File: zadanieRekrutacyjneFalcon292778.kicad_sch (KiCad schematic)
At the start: 65 parts, among them J1 Conn_01x03_Pin, J2 Conn_01x02_Pin, J3 Conn_01x02_Pin, J4 Conn_01x04_Pin, J5 Conn_01x08_Pin, J6 Conn_01x08_Pin, J7 Conn_01x02_Pin, SW1 CK_KMS2xxG, SW2 SW_Nidec_CAS-120A1, SW3 CK_KMS2xxG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

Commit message: placement + testowy tracking v1
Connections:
- net JTAGCLK: now also J4.1 (Pin_1); no longer J4.2 (Pin_2)
- net JTAGI: now also J4.3 (Pin_3); no longer J4.4 (Pin_4)
- net JTAGMS: now also J4.4 (Pin_4); no longer J4.1 (Pin_1)
- net JTAGO: now also J4.2 (Pin_2); no longer J4.3 (Pin_3)
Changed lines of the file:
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@@
-		)
-	)
-	(label "JTAGI"
-		(at 369.57 105.41 0)
-		(effects
-			(font
-				(size 1.27 1.27)
-			)
-			(justify left bottom)
 		)
 	)
@@
 		)
 	)
+	(label "JTAGI"
+		(at 369.57 102.87 0)
+		(effects
+			(font
+				(size 1.27 1.27)
+			)
+			(justify left bottom)
+		)
+	)
 	(label "SPI2"
 		(at 270.51 198.12 180)
@@
 		)
 	)
-	(label "JTAGCLK"
-		(at 369.57 100.33 0)
-		(effects
-			(font
-				(size 1.27 1.27)
-			)
-			(justify left bottom)
-		)
-	)
 	(label "JTAGO"
 		(at 190.5 86.36 0)
@@
 		)
 	)
-	(label "JTAGO"
-		(at 369.57 102.87 0)
-		(effects
-			(font
-				(size 1.27 1.27)
-			)
-			(justify left bottom)
-		)
-	)
 	(label "GPIO1"
 		(at 142.24 68.58 180)
@@
 		)
 	)
+	(label "JTAGCLK"
+		(at 369.57 97.79 0)
+		(effects
+			(font
+				(size 1.27 1.27)
+			)
+			(justify left bottom)
+		)
+	)
 	(label "SPICLK"
 		(at 270.51 190.5 180)
@@
 		)
 	)
-	(label "JTAGMS"
-		(at 369.57 97.79 0)
-		(effects
-			(font
-				(size 1.27 1.27)
-			)
-			(justify left bottom)
-		)
-	)
 	(label "IMUData"
 		(at 312.42 53.34 0)
@@
 		)
 	)
+	(label "JTAGMS"
+		(at 369.57 105.41 0)
+		(effects
+			(font
+				(size 1.27 1.27)
+			)
+			(justify left bottom)
+		)
+	)
 	(label "GPIO2"
 		(at 142.24 71.12 180)
@@
 		(effects
 			(font
+				(size 1.27 1.27)
+			)
+			(justify left bottom)
+		)
+	)
+	(label "JTAGO"
+		(at 369.57 100.33 0)
+		(effects
+			(font

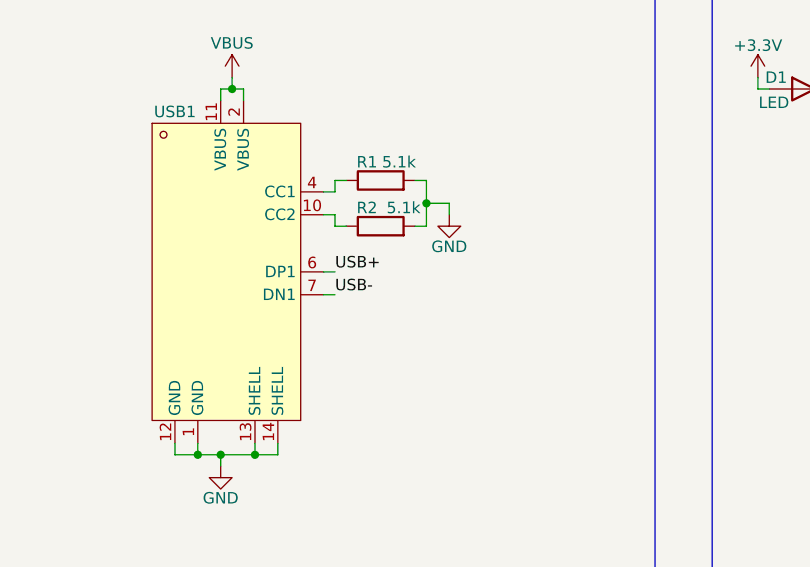
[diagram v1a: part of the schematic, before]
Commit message: zroutowane (do poprawy footprinty, DRC)
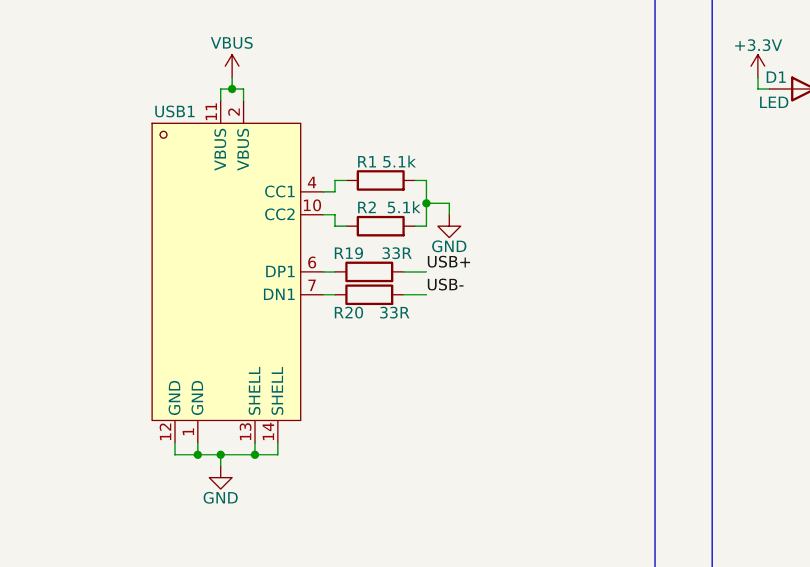
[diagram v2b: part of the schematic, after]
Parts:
- added R19, R20: 33R, Resistor_SMD:R_0603_1608Metric, symbol Device:R
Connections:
- net USB+: now also R19.2; no longer USB1.6 (DP1)
- net USB-: now also R20.2; no longer USB1.7 (DN1)
- new net: R19.1, USB1.6 (DP1)
- new net: R20.1, USB1.7 (DN1)
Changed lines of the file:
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@@
 	(wire
 		(pts
+			(xy 73.66 55.88) (xy 76.2 55.88)
+		)
+		(stroke
+			(width 0)
+			(type default)
+		)
+	)
+	(wire
+		(pts
 			(xy 189.23 86.36) (xy 190.5 86.36)
 		)
@@
 	(wire
 		(pts
+			(xy 73.66 53.34) (xy 76.2 53.34)
+		)
+		(stroke
+			(width 0)
+			(type default)
+		)
+	)
+	(wire
+		(pts
 			(xy 76.2 48.26) (xy 76.2 45.72)
 		)
@@
 	)
 	(label "USB-"
-		(at 66.04 55.88 0)
+		(at 76.2 55.88 0)
 		(effects
 			(font
@@
 	)
 	(label "USB+"
-		(at 66.04 53.34 0)
+		(at 76.2 53.34 0)
 		(effects
 			(font
@@
 	)
 	(symbol
+		(lib_id "Device:R")
+		(at 69.85 53.34 90)
+		(unit 1)
+		(exclude_from_sim no)
+		(in_bom yes)
+		(on_board yes)
+		(dnp no)
+		(property "Reference" "R19"
+			(at 67.564 51.308 90)
+			(effects
+				(font
+					(size 1.27 1.27)
+				)
+			)
+		)
+		(property "Value" "33R"
+			(at 72.898 51.308 90)
+			(effects
+				(font
+					(size 1.27 1.27)
+				)
+			)
+		)
+		(property "Footprint" "Resistor_SMD:R_0603_1608Metric"
+			(at 69.85 55.118 90)
+			(effects
+				(font
+					(size 1.27 1.27)
+				)
+				(hide yes)
+			)
+		)
+		(property "Datasheet" "~"
+			(at 69.85 53.34 0)
+			(effects
+				(font
+					(size 1.27 1.27)
+				)
+				(hide yes)
+			)
+		)
+		(property "Description" "Resistor"
+			(at 69.85 53.34 0)
+			(effects
+				(font
+					(size 1.27 1.27)
+				)
+				(hide yes)
+			)
+		)
+		(pin "1"
+		)
+		(pin "2"
+		)
+		(instances
+			(project "zadanieRekrutacyjneFalcon292778"
+				(path "/b0ec743d-f62d-4025-8f04-7134197de925"
+					(reference "R19")
+					(unit 1)
+				)
+			)
+		)
+	)
+	(symbol
 		(lib_id "Device:C")
 		(at 59.69 198.12 0)
@@
 					(unit 1)
 				)
+			)
+		)
+	)
+	(symbol
+		(lib_id "Device:R")
+		(at 69.85 55.88 90)
+		(unit 1)
+		(exclude_from_sim no)
+		(in_bom yes)
+		(on_board yes)
+		(dnp no)
+		(property "Reference" "R20"
+			(at 67.564 57.912 90)
+			(effects
+				(font
+					(size 1.27 1.27)
+				)
+			)
+		)
+		(property "Value" "33R"
+			(at 72.644 57.912 90)
+			(effects
+				(font
+					(size 1.27 1.27)
+				)
+			)
+		)
+		(property "Footprint" "Resistor_SMD:R_0603_1608Metric"
+			(at 69.85 57.658 90)
+			(effects
+				(font
+					(size 1.27 1.27)
+				)
+				(hide yes)
+			)
+		)
+		(property "Datasheet" "~"
+			(at 69.85 55.88 0)
+			(effects
+				(font
+					(size 1.27 1.27)
+				)
+				(hide yes)
+			)
+		)
+		(property "Description" "Resistor"
+			(at 69.85 55.88 0)
+			(effects
+				(font
+					(size 1.27 1.27)
+				)
+				(hide yes)
+			)
+		)
+		(pin "1"
+		)
+		(pin "2"
+		)
+		(instances
+			(project "zadanieRekrutacyjneFalcon292778"
+				(path "/b0ec743d-f62d-4025-8f04-7134197de925"
+					(reference "R20")
+					(unit 1)
+				)

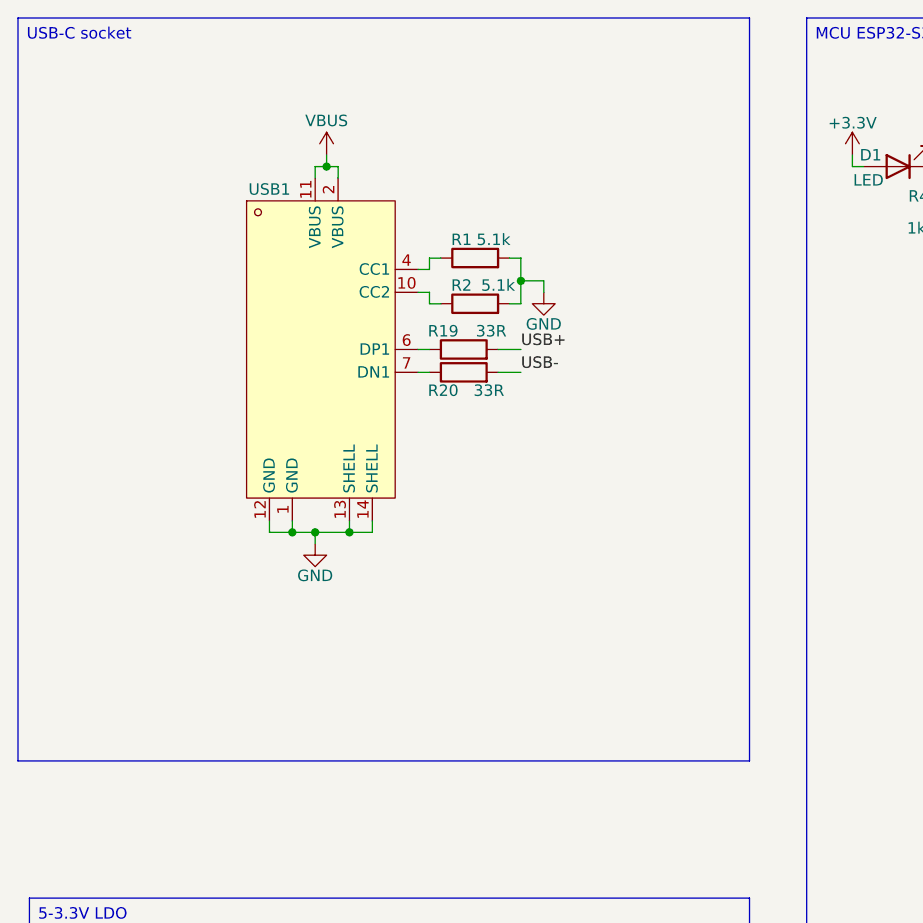
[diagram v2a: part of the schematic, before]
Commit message: DRC naprawione 3d modele dodane, transile dodane
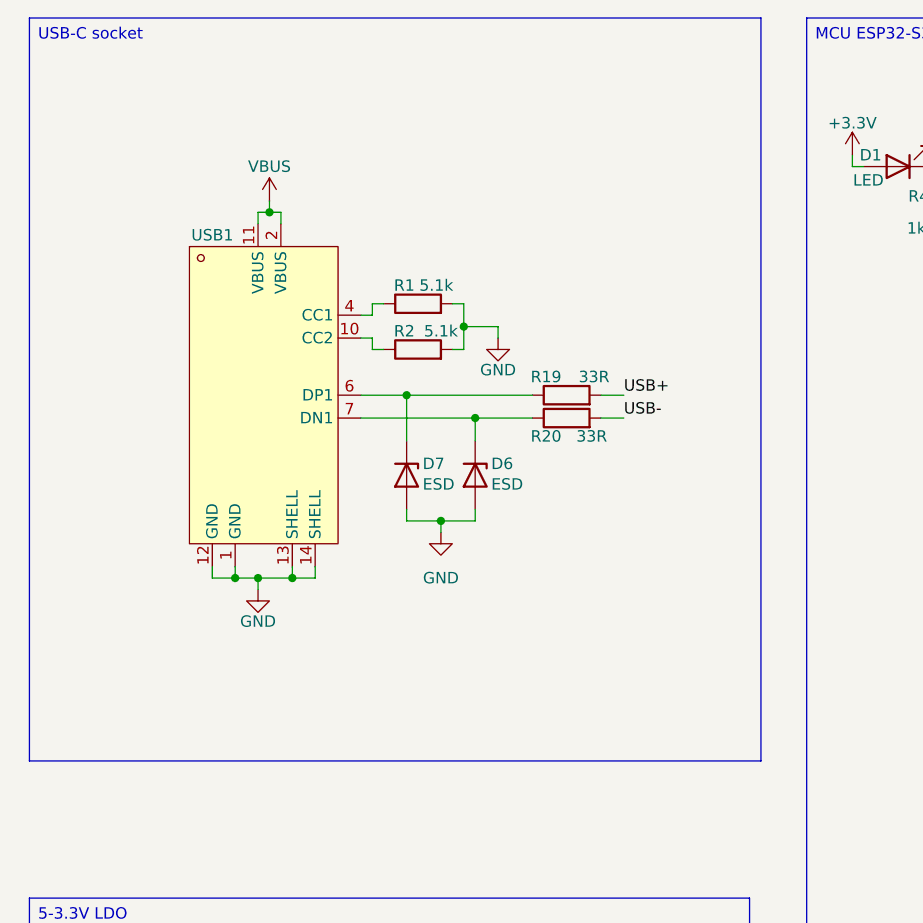
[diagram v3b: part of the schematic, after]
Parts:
- added D6, D7: ESD, Diode_SMD:D_SOD-523, symbol Diode:ESD5Zxx
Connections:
- net GND: now also D6.2 (A), D7.2 (A)
- net at R19.1, USB1.6 (DP1): now also D7.1 (K)
- net at R20.1, USB1.7 (DN1): now also D6.1 (K)
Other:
- moved on the sheet: R1, R19, R2, R20, USB1

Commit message: Finalna wersja v1
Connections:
- net GND: now also AE1.2 (GND)
- net Wi-Fi: no longer D2.2 (A2)
- net at AE1.1 (A), C14.1, L2.1: now also D2.2 (A2)
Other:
- moved on the sheet: C14, C15, D2, L2
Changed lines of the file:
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@@
 	)
 	(junction
+		(at 154.94 203.2)
+		(diameter 0)
+		(color 0 0 0 0)
+	)
+	(junction
 		(at 48.26 38.1)
 		(diameter 0)
@@
 	)
 	(junction
-		(at 165.1 193.04)
-		(diameter 0)
-		(color 0 0 0 0)
-	)
-	(junction
 		(at 69.85 132.08)
 		(diameter 0)
@@
 	)
 	(junction
-		(at 165.1 203.2)
+		(at 163.83 203.2)
 		(diameter 0)
 		(color 0 0 0 0)
@@
 	)
 	(junction
+		(at 163.83 193.04)
+		(diameter 0)
+		(color 0 0 0 0)
+	)
+	(junction
 		(at 39.37 193.04)
 		(diameter 0)
@@
 	)
 	(junction
+		(at 154.94 193.04)
+		(diameter 0)
+		(color 0 0 0 0)
+	)
+	(junction
 		(at 46.99 78.74)
 		(diameter 0)
@@
 	)
 	(junction
-		(at 154.94 193.04)
-		(diameter 0)
-		(color 0 0 0 0)
-	)
-	(junction
 		(at 67.31 72.39)
 		(diameter 0)
@@
 	(wire
 		(pts
-			(xy 173.99 194.31) (xy 173.99 193.04)
-		)
-		(stroke
-			(width 0)
-			(type default)
-		)
-	)
-	(wire
-		(pts
 			(xy 300.99 52.07) (xy 300.99 53.34)
 		)
@@
 	(wire
 		(pts
-			(xy 154.94 193.04) (xy 154.94 194.31)
+			(xy 163.83 193.04) (xy 163.83 194.31)
 		)
 		(stroke
@@
 	(wire
 		(pts
-			(xy 154.94 201.93) (xy 154.94 203.2)
+			(xy 163.83 201.93) (xy 163.83 203.2)
 		)
 		(stroke
@@
 	(wire
 		(pts
-			(xy 154.94 193.04) (xy 156.21 193.04)
+			(xy 123.19 48.26) (xy 123.19 49.53)
 		)
 		(stroke
@@
 	(wire
 		(pts
-			(xy 123.19 48.26) (xy 123.19 49.53)
+			(xy 281.94 175.26) (xy 281.94 177.8)
 		)
 		(stroke
@@
 	(wire
 		(pts
-			(xy 281.94 175.26) (xy 281.94 177.8)
+			(xy 189.23 83.82) (xy 190.5 83.82)
 		)
 		(stroke
@@
 	(wire
 		(pts
-			(xy 189.23 83.82) (xy 190.5 83.82)
+			(xy 68.58 193.04) (xy 68.58 194.31)
 		)
 		(stroke
@@
 	(wire
 		(pts
-			(xy 68.58 193.04) (xy 68.58 194.31)
+			(xy 44.45 78.74) (xy 46.99 78.74)
 		)
 		(stroke
@@
 	(wire
 		(pts
-			(xy 44.45 78.74) (xy 46.99 78.74)
+			(xy 189.23 88.9) (xy 190.5 88.9)
 		)
 		(stroke
@@
 	(wire
 		(pts
-			(xy 189.23 88.9) (xy 190.5 88.9)
+			(xy 173.99 203.2) (xy 170.18 203.2)
 		)
 		(stroke
@@
 	(wire
 		(pts
-			(xy 154.94 203.2) (xy 165.1 203.2)
+			(xy 163.83 203.2) (xy 170.18 203.2)
 		)
 		(stroke
@@
 	(wire
 		(pts
-			(xy 163.83 193.04) (xy 165.1 193.04)
+			(xy 172.72 193.04) (xy 173.99 193.04)
 		)
 		(stroke
@@
 	(wire
 		(pts
-			(xy 173.99 193.04) (xy 165.1 193.04)
+			(xy 142.24 66.04) (xy 143.51 66.04)
 		)
 		(stroke
@@
 	(wire
 		(pts
-			(xy 142.24 66.04) (xy 143.51 66.04)
+			(xy 142.24 68.58) (xy 143.51 68.58)
 		)
 		(stroke
@@
 	(wire
 		(pts
-			(xy 142.24 68.58) (xy 143.51 68.58)
+			(xy 152.4 203.2) (xy 154.94 203.2)
 		)
 		(stroke
@@
 	(wire
 		(pts
-			(xy 165.1 193.04) (xy 165.1 194.31)
+			(xy 173.99 193.04) (xy 173.99 194.31)
 		)
 		(stroke
@@
 	(wire
 		(pts
-			(xy 165.1 203.2) (xy 170.18 203.2)
-		)
-		(stroke
-			(width 0)
-			(type default)
-		)
-	)
-	(wire
-		(pts
 			(xy 63.5 58.42) (xy 63.5 63.5)
 		)
@@
 	(wire
 		(pts
+			(xy 163.83 193.04) (xy 165.1 193.04)
+		)
+		(stroke
+			(width 0)
+			(type default)
+		)
+	)
+	(wire
+		(pts
 			(xy 64.77 142.24) (xy 69.85 142.24)
 		)
@@
 	(wire
 		(pts
-			(xy 165.1 201.93) (xy 165.1 203.2)
+			(xy 142.24 73.66) (xy 143.51 73.66)
 		)
 		(stroke
@@
 	(wire
 		(pts
-			(xy 142.24 73.66) (xy 143.51 73.66)
+			(xy 154.94 193.04) (xy 154.94 194.31)
 		)
 		(stroke
@@
 	(wire
 		(pts
+			(xy 154.94 201.93) (xy 154.94 203.2)
+		)
+		(stroke
+			(width 0)
+			(type default)
+		)
+	)
+	(wire
+		(pts
 			(xy 52.07 132.08) (xy 53.34 132.08)
 		)
@@
 	(wire
 		(pts
+			(xy 163.83 193.04) (xy 154.94 193.04)
+		)
+		(stroke
+			(width 0)
+			(type default)
+		)
+	)
+	(wire
+		(pts
 			(xy 300.99 53.34) (xy 312.42 53.34)
 		)
@@
 	(wire
 		(pts
+			(xy 154.94 203.2) (xy 163.83 203.2)
+		)
+		(stroke
+			(width 0)
+			(type default)
+		)
+	)
+	(wire
+		(pts
 			(xy 142.24 93.98) (xy 143.51 93.98)
 		)
@@
 	(wire
 		(pts
-			(xy 170.18 203.2) (xy 173.99 203.2)
+			(xy 152.4 190.5) (xy 152.4 203.2)
 		)
 		(stroke
@@
 	(symbol
 		(lib_id "Device:C")
-		(at 154.94 198.12 0)
+		(at 163.83 198.12 0)
 		(unit 1)
 		(exclude_from_sim no)
@@
 		(dnp no)
 		(property "Reference" "C14"
-			(at 156.464 195.58 0)
+			(at 165.354 195.58 0)
 			(effects
 				(font
@@
 		)
 		(property "Value" "C"
-			(at 156.972 200.914 0)
+			(at 165.862 200.914 0)
 			(effects
 				(font
@@
 		)
 		(property "Footprint" "Capacitor_SMD:C_0603_1608Metric"
-			(at 155.9052 201.93 0)
+			(at 164.7952 201.93 0)
 			(effects
 				(font
@@
 		)
 		(property "Datasheet" "~"
-			(at 154.94 198.12 0)
+			(at 163.83 198.12 0)
 			(effects
 				(font
@@
 		)
 		(property "Description" "Unpolarized capacitor"
-			(at 154.94 198.12 0)
+			(at 163.83 198.12 0)
 			(effects
 				(font
@@
 	(symbol
 		(lib_id "Device:C")
-		(at 165.1 198.12 0)
+		(at 173.99 198.12 0)
 		(unit 1)
 		(exclude_from_sim no)
@@
 		(dnp no)
 		(property "Reference" "C15"
-			(at 167.132 195.834 0)
+			(at 176.022 195.834 0)
 			(effects
 				(font
@@
 		)
 		(property "Value" "C"
-			(at 168.148 201.168 0)
+			(at 177.038 201.168 0)
 			(effects
 				(font
@@
 		)
 		(property "Footprint" "Capacitor_SMD:C_0603_1608Metric"
-			(at 166.0652 201.93 0)
+			(at 174.9552 201.93 0)
 			(effects
 				(font
@@
 		)
 		(property "Datasheet" "~"
-			(at 165.1 198.12 0)
+			(at 173.99 198.12 0)
 			(effects
 				(font
@@
 		)
 		(property "Description" "Unpolarized capacitor"
-			(at 165.1 198.12 0)
+			(at 173.99 198.12 0)
 			(effects
 				(font
@@
 	(symbol
 		(lib_id "Device:D_TVS")
-		(at 173.99 198.12 90)
+		(at 154.94 198.12 90)
 		(unit 1)
 		(exclude_from_sim no)
@@
 		(dnp no)
 		(property "Reference" "D2"
-			(at 176.53 195.834 90)
+			(at 157.48 195.834 90)
 			(effects
 				(font
@@
 		)
 		(property "Value" "D_TVS"
-			(at 176.53 200.66 90)
+			(at 157.48 200.66 90)
 			(effects
 				(font
@@
 		)
 		(property "Footprint" "Package_SON:Texas_DPY0002A_0.6x1mm_P0.65mm"
-			(at 173.99 198.12 0)
+			(at 154.94 198.12 0)
 			(effects
 				(font
@@
 		)
 		(property "Datasheet" "~"
-			(at 173.99 198.12 0)
+			(at 154.94 198.12 0)
 			(effects
 				(font
@@
 		)
 		(property "Description" "Bidirectional transient-voltage-suppression diode"
-			(at 173.99 198.12 0)
+			(at 154.94 198.12 0)
 			(effects
 				(font
@@
 		)
 		(instances
-			(project ""
+			(project "zadanieRekrutacyjneFalcon292778"
 				(path "/b0ec743d-f62d-4025-8f04-7134197de925"
 					(reference "D2")
@@
 	(symbol
 		(lib_id "Device:L")
-		(at 160.02 193.04 90)
+		(at 168.91 193.04 90)
 		(unit 1)
 		(exclude_from_sim no)
@@
 		(dnp no)
 		(property "Reference" "L2"
-			(at 157.48 190.754 90)
+			(at 166.37 190.754 90)
 			(effects
 				(font
@@
 		)
 		(property "Value" "L"
-			(at 161.798 190.754 90)
+			(at 170.688 190.754 90)
 			(effects
 				(font
@@
 		)
 		(property "Footprint" "Inductor_SMD:L_0603_1608Metric"
-			(at 160.02 193.04 0)
+			(at 168.91 193.04 0)
 			(effects
 				(font
@@
 		)
 		(property "Datasheet" "~"
-			(at 160.02 193.04 0)
+			(at 168.91 193.04 0)
 			(effects
 				(font
@@
 		)
 		(property "Description" "Inductor"
-			(at 160.02 193.04 0)
+			(at 168.91 193.04 0)
 			(effects
 				(font
@@
 		)
 		(property "Value" "Antenna"
-			(at 146.05 189.484 0)
+			(at 146.05 188.214 0)
 			(effects
 				(font
@@
 		(pin "1"
 		)
+		(pin "2"
+		)
 		(instances
